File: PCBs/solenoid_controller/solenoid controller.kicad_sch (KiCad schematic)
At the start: 22 parts

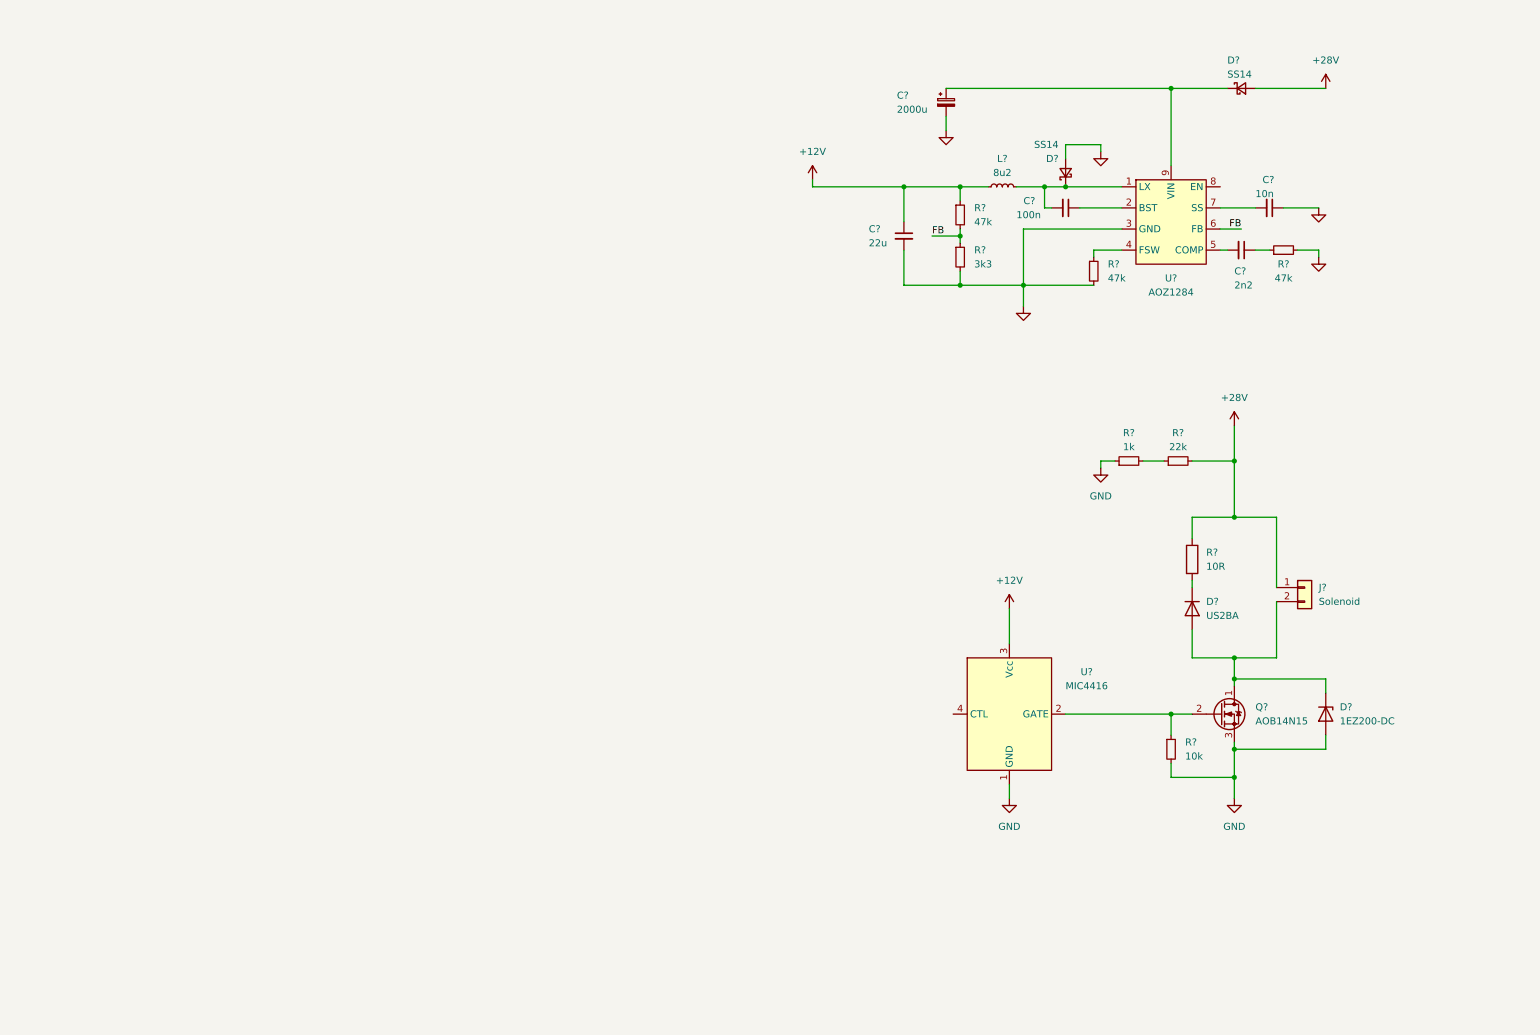
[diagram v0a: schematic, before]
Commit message: circuitry in progress + cubemx project for stm32
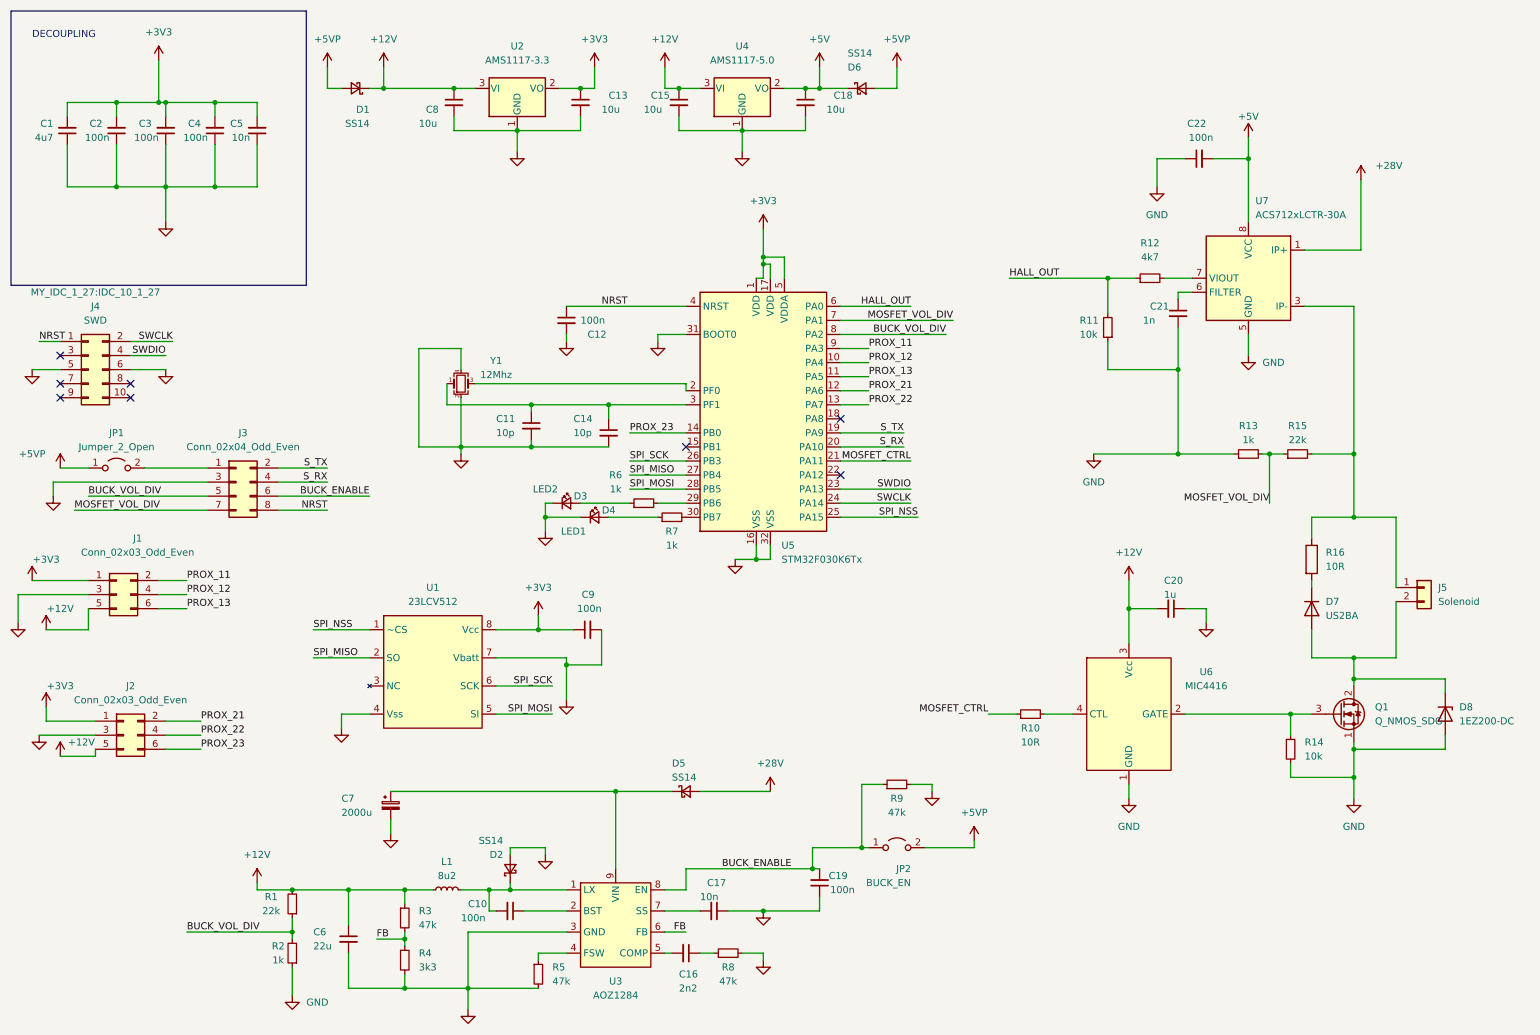
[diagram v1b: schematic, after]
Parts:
- removed C?: 10n, Capacitor_SMD:C_0603_1608Metric_Pad1.08x0.95mm_HandSolder, symbol Device:C_Small
- removed C?: 2n2, Capacitor_SMD:C_0603_1608Metric_Pad1.08x0.95mm_HandSolder, symbol Device:C_Small
- removed C?: 2000u, symbol Device:C_Polarized_Small
- removed C?: 22u, Capacitor_SMD:C_0805_2012Metric_Pad1.18x1.45mm_HandSolder, symbol Device:C_Small
- removed C?: 100n, Capacitor_SMD:C_0603_1608Metric_Pad1.08x0.95mm_HandSolder, symbol Device:C_Small
- removed D? (x2): SS14, Diode_SMD:D_SMA_Handsoldering, symbol Device:D_Schottky_Small
- removed L?: 8u2, Inductor_SMD:L_7.3x7.3_H4.5, symbol Device:L_Small
- removed Q?: AOB14N15, symbol Device:Q_NMOS_DGS
- removed R?: 3k3, Resistor_SMD:R_0603_1608Metric_Pad0.98x0.95mm_HandSolder, symbol Device:R_Small
- removed R? (x3): 47k, Resistor_SMD:R_0603_1608Metric_Pad0.98x0.95mm_HandSolder, symbol Device:R_Small
- removed U?: AOZ1284, MY_BLUETOOTH:SO-8-pad, symbol My_Buck:AOZ1284
- added C1: 4u7, Capacitor_SMD:C_0603_1608Metric_Pad1.08x0.95mm_HandSolder, symbol Device:C_Small
- added C10, C12, C19, C2, C22, C3, C4, C9: 100n, Capacitor_SMD:C_0603_1608Metric_Pad1.08x0.95mm_HandSolder, symbol Device:C_Small
- added C11, C14: 10p, Capacitor_SMD:C_0603_1608Metric_Pad1.08x0.95mm_HandSolder, symbol Device:C_Small
- added C13, C15, C18, C8: 10u, Capacitor_SMD:C_0603_1608Metric_Pad1.08x0.95mm_HandSolder, symbol Device:C_Small
- added C16: 2n2, Capacitor_SMD:C_0603_1608Metric_Pad1.08x0.95mm_HandSolder, symbol Device:C_Small
- added C17, C5: 10n, Capacitor_SMD:C_0603_1608Metric_Pad1.08x0.95mm_HandSolder, symbol Device:C_Small
- added C20: 1u, Capacitor_SMD:C_0603_1608Metric_Pad1.08x0.95mm_HandSolder, symbol Device:C_Small
- added C21: 1n, Capacitor_SMD:C_0603_1608Metric_Pad1.08x0.95mm_HandSolder, symbol Device:C_Small
- added C6: 22u, Capacitor_SMD:C_0805_2012Metric_Pad1.18x1.45mm_HandSolder, symbol Device:C_Small
- added C7: 2000u, Capacitor_THT:CP_Radial_D8.0mm_P3.50mm, symbol Device:C_Polarized_Small
- added D1, D2, D5, D6: SS14, Diode_SMD:D_SMA_Handsoldering, symbol Device:D_Schottky_Small
- added D3: LED2, LED_SMD:LED_0603_1608Metric_Pad1.05x0.95mm_HandSolder, symbol Device:LED_Small
- added D4: LED1, LED_SMD:LED_0603_1608Metric_Pad1.05x0.95mm_HandSolder, symbol Device:LED_Small
- added J1, J2: Conn_02x03_Odd_Even, Connector_IDC:IDC-Header_2x03_P2.54mm_Vertical, symbol Connector_Generic:Conn_02x03_Odd_Even
- added J3: Conn_02x04_Odd_Even, Connector_IDC:IDC-Header_2x04_P2.54mm_Vertical, symbol Connector_Generic:Conn_02x04_Odd_Even
- added J4: SWD, MY_IDC_1_27:IDC_10_1_27, symbol Connector_Generic:Conn_02x05_Odd_Even
- added JP1: Jumper_2_Open, Connector_PinHeader_2.54mm:PinHeader_1x02_P2.54mm_Vertical, symbol Jumper:Jumper_2_Open
- added JP2: BUCK_EN, Connector_PinHeader_2.54mm:PinHeader_1x02_P2.54mm_Vertical, symbol Jumper:Jumper_2_Open
- added L1: 8u2, Inductor_SMD:L_7.3x7.3_H4.5, symbol Device:L_Small
- added Q1: Q_NMOS_SDG, Package_TO_SOT_SMD:TO-263-2, symbol Device:Q_NMOS_SDG
- added R1: 22k, Resistor_SMD:R_0603_1608Metric_Pad0.98x0.95mm_HandSolder, symbol Device:R_Small
- added R10: 10R, Resistor_SMD:R_0603_1608Metric_Pad0.98x0.95mm_HandSolder, symbol Device:R_Small
- added R11: 10k, Resistor_SMD:R_0603_1608Metric_Pad0.98x0.95mm_HandSolder, symbol Device:R_Small
- added R12: 4k7, Resistor_SMD:R_0603_1608Metric_Pad0.98x0.95mm_HandSolder, symbol Device:R_Small
- added R2, R6, R7: 1k, Resistor_SMD:R_0603_1608Metric_Pad0.98x0.95mm_HandSolder, symbol Device:R_Small
- added R3, R5, R8, R9: 47k, Resistor_SMD:R_0603_1608Metric_Pad0.98x0.95mm_HandSolder, symbol Device:R_Small
- added R4: 3k3, Resistor_SMD:R_0603_1608Metric_Pad0.98x0.95mm_HandSolder, symbol Device:R_Small
- added U1: 23LCV512, Package_SO:SO-8_5.3x6.2mm_P1.27mm, symbol My elements:23LCV512
- added U2: AMS1117-3.3, Package_TO_SOT_SMD:SOT-223-3_TabPin2, symbol Regulator_Linear:AMS1117-3.3
- added U3: AOZ1284, MY_BLUETOOTH:SO-8-pad, symbol My_Buck:AOZ1284
- added U4: AMS1117-5.0, Package_TO_SOT_SMD:SOT-223-3_TabPin2, symbol Regulator_Linear:AMS1117-5.0
- added U5: STM32F030K6Tx, Package_QFP:LQFP-32_7x7mm_P0.8mm, symbol MCU_ST_STM32F0:STM32F030K6Tx
- added U7: ACS712xLCTR-30A, Package_SO:SOIC-8_3.9x4.9mm_P1.27mm, symbol Sensor_Current:ACS712xLCTR-30A
- added Y1: 12Mhz, Crystal:Crystal_SMD_3225-4Pin_3.2x2.5mm_HandSoldering, symbol Device:Crystal_GND24_Small
- J5: renamed from J?; footprint (none) -> Inductor_SMD:L_Bourns_SRR1208_12.7x12.7mm
- R13, R15: renamed from R?; footprint (none) -> Resistor_SMD:R_0603_1608Metric_Pad0.98x0.95mm_HandSolder
- gave numbers to parts that had none: 5
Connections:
- net +12V: now also C15.1, C20.2, C6.1, C8.1, D1.1 (K), J1.5 (Pin_5), J2.5 (Pin_5), L1.1, R1.2, R3.1, U2.3 (VI), U4.3 (VI)
- net +28V: now also D5.2 (A), U7.1 (IP+), U7.2 (IP+); no longer J5.1 (Pin_1), R15.2, R16.1
- net FB: now also R3.2, R4.1, U3.6 (FB)
- net GND: now also C1.1, C11.2, C12.2, C13.2, C14.2, C15.2, C17.1, C18.2, C19.1, C2.1, C20.1, C21.2, C22.1, C3.1, C4.1, C5.1, C6.2, C7.2, C8.2, C9.2, D2.2 (A), D3.1 (K), D4.1 (K), J1.3 (Pin_3), J2.3 (Pin_3), J3.3 (Pin_3), J4.5 (Pin_5), J4.6 (Pin_6), Q1.1 (S), R11.1, R2.1, R4.2, R5.2, R8.2, R9.2, U1.4 (Vss), U1.7 (Vbatt), U2.1 (GND), U3.3 (GND), U4.1 (GND), U5.16 (VSS), U5.31 (BOOT0), U5.32 (VSS), U7.5 (GND), Y1.2, Y1.4
- net at R14.1, U6.2 (GATE): now also Q1.3 (G)
- net at D7.2 (A), D8.1 (K), J5.2 (Pin_2): now also Q1.2 (D)
- net MOSFET_VOL_DIV: now reaches R13.2, R15.1
- net MOSFET_VOL_DIV: now also J3.7 (Pin_7), U5.7 (PA1)
- net at U6.4 (CTL): now also R10.2
- new net: R12.2, U7.7 (VIOUT)
- new net: C10.1, U3.2 (BST)
- new net: C10.2, D2.1 (K), L1.2, U3.1 (LX)
- new net: C16.1, R8.1
- new net: C16.2, U3.5 (COMP)
- new net: D4.2 (A), R7.1
- new net: J5.1 (Pin_1), R15.2, R16.1, U7.3 (IP-), U7.4 (IP-)
- new net: C11.1, C14.1, U5.3 (PF1), Y1.1
- new net: U5.2 (PF0), Y1.3
- new net: J3.1 (Pin_1), JP1.2 (B)
- new net: R7.2, U5.30 (PB7)
- new net: R5.1, U3.4 (FSW)
- new net: C17.2, U3.7 (SS)
- new net: C7.1, D5.1 (K), U3.9 (VIN)
- new net: D3.2 (A), R6.1
- new net: R6.2, U5.29 (PB6)
- new net: C21.1, U7.6 (FILTER)
- new net +3V3: C1.2, C13.1, C2.2, C3.2, C4.2, C5.2, C9.1, J1.1 (Pin_1), J2.1 (Pin_1), U1.8 (Vcc), U2.2 (VO), U5.1 (VDD), U5.17 (VDD), U5.5 (VDDA)
- new net +5V: C18.1, C22.2, D6.1 (K), U4.2 (VO), U7.8 (VCC)
- new net +5VP: D1.2 (A), D6.2 (A), JP1.1 (A), JP2.2 (B)
- new net BUCK_ENABLE: C19.2, J3.6 (Pin_6), JP2.1 (A), R9.1, U3.8 (EN)
- new net BUCK_VOL_DIV: J3.5 (Pin_5), R1.1, R2.2, U5.8 (PA2)
- new net HALL_OUT: R11.2, R12.1, U5.6 (PA0)
- new net MOSFET_CTRL: R10.1, U5.21 (PA11)
- new net NRST: C12.1, J3.8 (Pin_8), J4.1 (Pin_1), U5.4 (NRST)
- new net PROX_11: J1.2 (Pin_2), U5.9 (PA3)
- new net PROX_12: J1.4 (Pin_4), U5.10 (PA4)
- new net PROX_13: J1.6 (Pin_6), U5.11 (PA5)
- new net PROX_21: J2.2 (Pin_2), U5.12 (PA6)
- new net PROX_22: J2.4 (Pin_4), U5.13 (PA7)
- new net PROX_23: J2.6 (Pin_6), U5.14 (PB0)
- new net SPI_MISO: U1.2 (SO), U5.27 (PB4)
- new net SPI_MOSI: U1.5 (SI), U5.28 (PB5)
- new net SPI_NSS: U1.1 (~CS), U5.25 (PA15)
- new net SPI_SCK: U1.6 (SCK), U5.26 (PB3)
- new net SWCLK: J4.2 (Pin_2), U5.24 (PA14)
- new net SWDIO: J4.4 (Pin_4), U5.23 (PA13)
- new net S_RX: J3.4 (Pin_4), U5.20 (PA10)
- new net S_TX: J3.2 (Pin_2), U5.19 (PA9)
- no-connect marks 0 -> 8
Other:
- note added: "DECOUPLING"
- moved on the sheet: D7, D8, J5, R13, R14, R15, R16, U6

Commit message: PCB update
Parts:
- added J6: GND_CONN, My_elements:single_PAD, symbol Connector:Conn_01x01_Pin
- added J7: 28V_CONN, My_elements:single_PAD, symbol Connector:Conn_01x01_Pin
- added R17: 1k, Resistor_SMD:R_0603_1608Metric_Pad0.98x0.95mm_HandSolder, symbol Device:R_Small
- C13, C15, C18, C8: footprint Capacitor_SMD:C_0603_1608Metric_Pad1.08x0.95mm_HandSolder -> Capacitor_SMD:C_0805_2012Metric_Pad1.18x1.45mm_HandSolder
- D7: footprint Diode_SMD:D_SMA -> Diode_SMD:D_SMA_Handsoldering
- R1: value 22k -> 10k
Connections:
- net +28V: now also J7.1 (Pin_1)
- net +5VP: now also R17.2; no longer JP2.2 (B)
- net GND: now also J6.1 (Pin_1)
- net at C14.1, U5.3 (PF1), Y1.1: no longer C11.1
- net at U5.2 (PF0), Y1.3: now also C11.1
- new net: JP2.2 (B), R17.1
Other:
- moved on the sheet: J1
